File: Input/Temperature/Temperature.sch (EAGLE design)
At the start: 10 parts, among them U5 TMP006AIYZFR

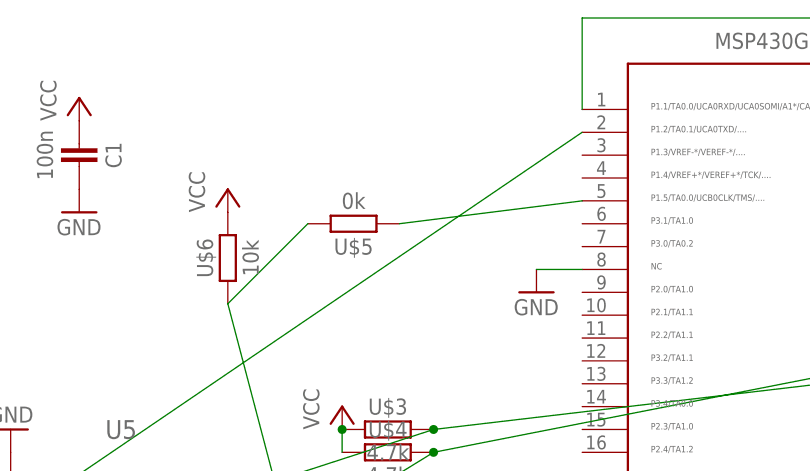
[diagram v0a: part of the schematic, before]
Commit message: Update Pinheader
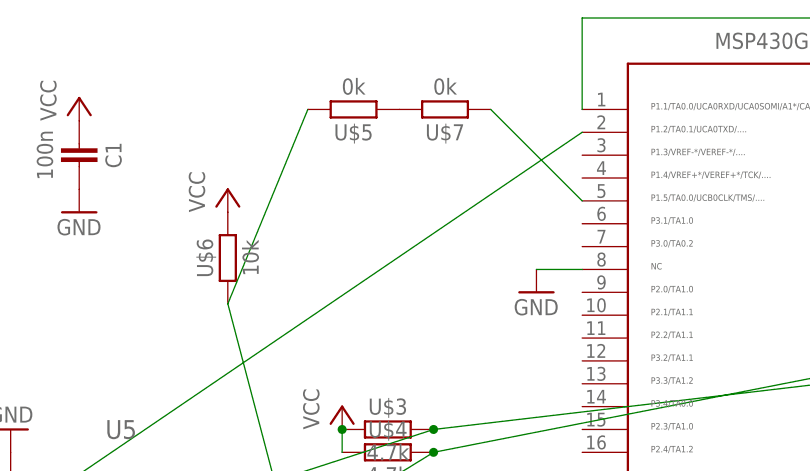
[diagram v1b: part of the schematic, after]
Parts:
- added U$7: 0k, thar:RESISTOR0603
- U$5: device thar:RESISTOR1206 -> thar:RESISTOR0603
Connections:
- new net N$11: U$5.1, U$7.2
- net N$2: now also U$7.1; no longer U$5.1
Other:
- moved on the sheet: U$5
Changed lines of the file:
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@@
 <part name="P+7" library="supply1" deviceset="VCC" device=""/>
 <part name="C2" library="thar" deviceset="CAPACITOR" device="" value="100n"/>
-<part name="U$5" library="thar" deviceset="RESISTOR" device="1206" value="0k"/>
+<part name="U$5" library="thar" deviceset="RESISTOR" device="0603" value="0k"/>
 <part name="P+1" library="supply1" deviceset="VCC" device=""/>
 <part name="GND7" library="supply1" deviceset="GND" device=""/>
+<part name="U$7" library="thar" deviceset="RESISTOR" device="0603" value="0k"/>
 </parts>
 <sheets>
@@
 <instance part="P+7" gate="VCC" x="36.83" y="107.95"/>
 <instance part="C2" gate="G$1" x="12.7" y="73.66" rot="R270"/>
-<instance part="U$5" gate="G$1" x="50.8" y="104.14" rot="R180"/>
+<instance part="U$5" gate="G$1" x="50.8" y="116.84" rot="R180"/>
 <instance part="P+1" gate="VCC" x="152.4" y="106.68"/>
 <instance part="GND7" gate="1" x="144.78" y="104.14"/>
+<instance part="U$7" gate="G$1" x="60.96" y="116.84" rot="R180"/>
 </instances>
 <busses>
@@
 <pinref part="U$6" gate="G$1" pin="1"/>
 <pinref part="U$5" gate="G$1" pin="2"/>
-<wire x1="45.72" y1="104.14" x2="36.83" y2="95.25" width="0.1524" layer="91"/>
+<wire x1="45.72" y1="116.84" x2="36.83" y2="95.25" width="0.1524" layer="91"/>
 </segment>
 </net>
@@
 <segment>
 <pinref part="U$10" gate="G$1" pin="5"/>
+<pinref part="U$7" gate="G$1" pin="1"/>
+<wire x1="66.04" y1="116.84" x2="76.2" y2="106.68" width="0.1524" layer="91"/>
+</segment>
+</net>
+<net name="N$11" class="0">
+<segment>
 <pinref part="U$5" gate="G$1" pin="1"/>
-<wire x1="76.2" y1="106.68" x2="55.88" y2="104.14" width="0.1524" layer="91"/>
-</segment>
-</net>
+<pinref part="U$7" gate="G$1" pin="2"/>
+</segment>
+</net>
